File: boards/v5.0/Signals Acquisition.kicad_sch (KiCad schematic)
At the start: 11 parts, among them U3 PC817

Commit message: Update board v5.0 docs
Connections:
- net GND renamed Earth
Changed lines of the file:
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@@
   (junction (at 74.93 92.71) (diameter 0) (color 0 0 0 0)
   )
+  (junction (at 123.19 74.93) (diameter 0) (color 0 0 0 0)
+  )
   (junction (at 113.03 74.93) (diameter 0) (color 0 0 0 0)
   )
@@
     (stroke (width 0) (type default))
   )
+  (wire (pts (xy 123.19 74.93) (xy 123.19 76.2))
+    (stroke (width 0) (type default))
+  )
   (wire (pts (xy 74.93 92.71) (xy 76.2 92.71))
     (stroke (width 0) (type default))
   )
-  (wire (pts (xy 111.76 69.85) (xy 121.92 69.85))
+  (wire (pts (xy 111.76 69.85) (xy 124.46 69.85))
     (stroke (width 0) (type default))
   )
@@
     (stroke (width 0) (type default))
   )
+  (wire (pts (xy 124.46 74.93) (xy 123.19 74.93))
+    (stroke (width 0) (type default))
+  )
   (wire (pts (xy 73.66 130.81) (xy 76.2 130.81))
     (stroke (width 0) (type default))
@@
   )
   (wire (pts (xy 85.09 78.74) (xy 86.36 78.74))
+    (stroke (width 0) (type default))
+  )
+  (wire (pts (xy 123.19 74.93) (xy 121.92 74.93))
     (stroke (width 0) (type default))
   )
@@
     (effects (font (size 1.27 1.27)) (justify left))
   )
-  (hierarchical_label "Vcc" (shape input) (at 121.92 69.85 0) (fields_autoplaced)
+  (hierarchical_label "Vcc" (shape input) (at 124.46 69.85 0) (fields_autoplaced)
     (effects (font (size 1.27 1.27)) (justify left))
   )
@@
     (effects (font (size 1.27 1.27)) (justify left))
   )
-  (hierarchical_label "GND" (shape input) (at 121.92 74.93 0) (fields_autoplaced)
+  (hierarchical_label "GND" (shape input) (at 124.46 74.93 0) (fields_autoplaced)
     (effects (font (size 1.27 1.27)) (justify left))
   )
@@
     )
   )
+  (symbol (lib_id "power:Earth") (at 123.19 76.2 0) (unit 1)
+    (in_bom yes) (on_board yes) (dnp no) (fields_autoplaced)
+    (property "Reference" "#PWR017" (at 123.19 82.55 0)
+      (effects (font (size 1.27 1.27)) hide)
+    )
+    (property "Value" "Earth" (at 123.19 80.01 0)
+      (effects (font (size 1.27 1.27)) hide)
+    )
+    (property "Footprint" "" (at 123.19 76.2 0)
+      (effects (font (size 1.27 1.27)) hide)
+    )
+    (property "Datasheet" "~" (at 123.19 76.2 0)
+      (effects (font (size 1.27 1.27)) hide)
+    )
+    (pin "1")
+    (instances
+      (project "board"
+        (path "/7fdecbff-7204-4ee7-8cff-285fbd7a00a8/99e862ea-0608-4359-a6b2-c0a50691ba5c"
+          (reference "#PWR017") (unit 1)
+        )
+      )
+    )
+  )
   (symbol (lib_id "Diode:1N4007") (at 81.28 78.74 0) (mirror x) (unit 1)
     (in_bom yes) (on_board yes) (dnp no)
@@
   (symbol (lib_id "Isolator:PC817") (at 104.14 72.39 0) (unit 1)
     (in_bom yes) (on_board yes) (dnp no)
-    (property "Reference" "U3" (at 104.14 80.01 0)
-      (effects (font (size 1.27 1.27)))
-    )
-    (property "Value" "PC817" (at 104.14 77.47 0)
-      (effects (font (size 1.27 1.27)))
-    )
+    (property "Reference" "U3" (at 104.14 64.77 0)
+      (effects (font (size 1.27 1.27)))
+    )
+    (property "Value" "PC817" (at 104.14 67.31 0)
+      (effects (font (size 1.27 1.27)))
+    )

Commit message: Update in the V5 board
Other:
- note removed: "-30 to +100"
- note removed: "-40 to +60"
- note removed: "0"
- note removed: "0 to +70"
- note removed: "0 to 1000"
- note removed: "1"
- note removed: "1 to 2"
- note removed: "127Vac"
- note removed: "180kΩ"
- note removed: "2"
- note removed: "220Vac"
- note removed: "3"
- note removed: "300kΩ"
- note removed: "380Vac"
- note removed: "440Vac"
- note removed: "470kΩ"
- note removed: "510kΩ"
- note removed: "After selecting the ideal resistor for your application, according to the table, remember to modify the value of the variable "VOLTAGE_TYPE" in the Microcomputer according to what's in the table"
- note removed: "Input Voltage Range"
- note removed: "Observation"
- note removed: "Operating Temperature Range"
- note removed: "PC817 Operation Temperature"
- note removed: "Rating"
- note removed: "Resistor to Voltage"
- note removed: "Rvolt"
- note removed: "Specifications"
- note removed: "System Voltage (RMS)"
- note removed: "Type"
- note removed: "Unit"
- note removed: "Vac"
- note removed: "Value"
- note removed: "ZMPT101B Nominal Current Range"
- note removed: "ZMPT101B Operation Temperature"
- note removed: "mA"
- note removed: "°C"

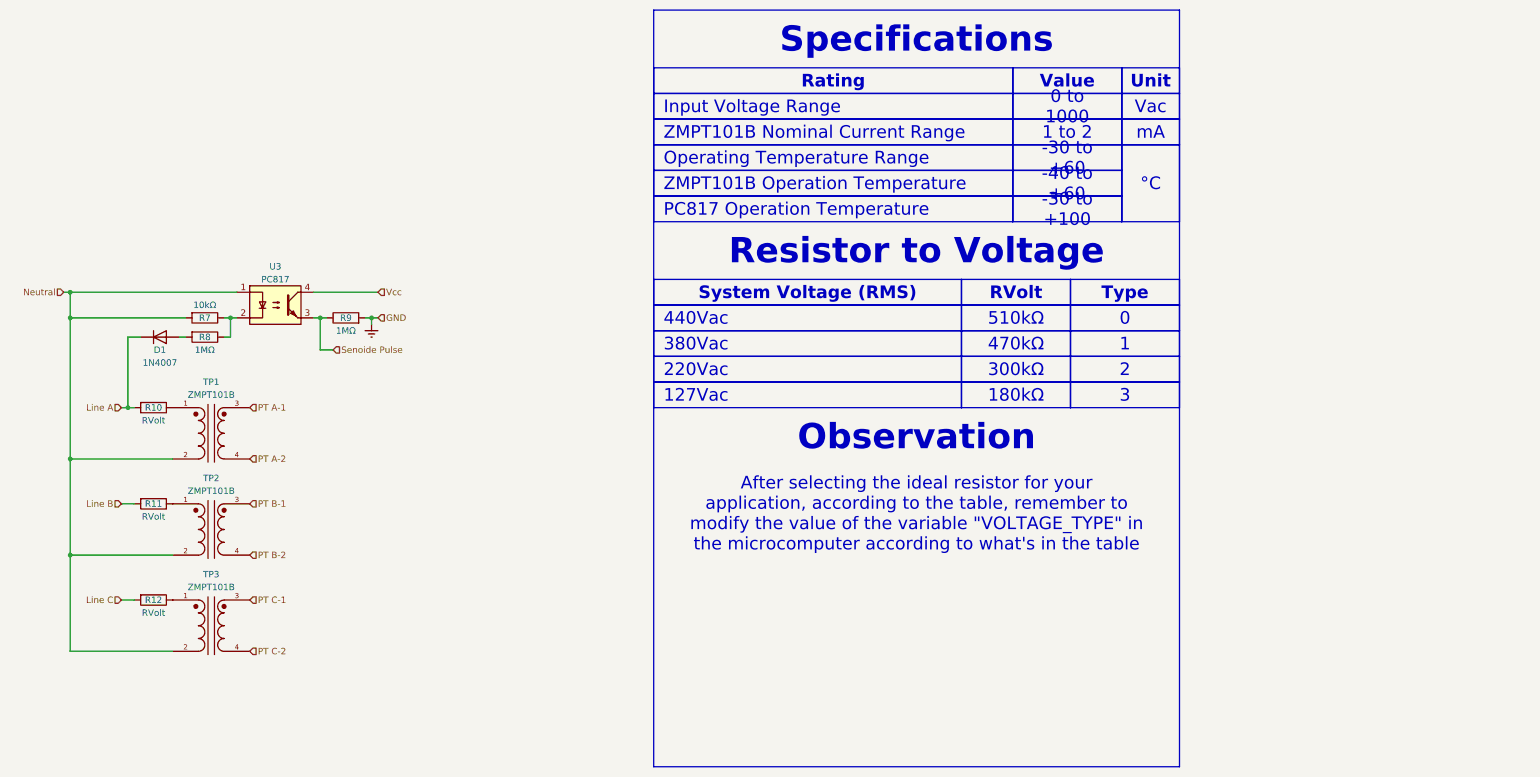
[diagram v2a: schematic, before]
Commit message: Add Jupyter notebook for calculating possible sample rates
- Introduced a new notebook `possible_sample_rates.ipynb` that calculates sample rates based on a base frequency of 60Hz.
- The notebook iterates through a range of values to compute and print sample rates, frequencies, microseconds, and remainders for specific conditions.
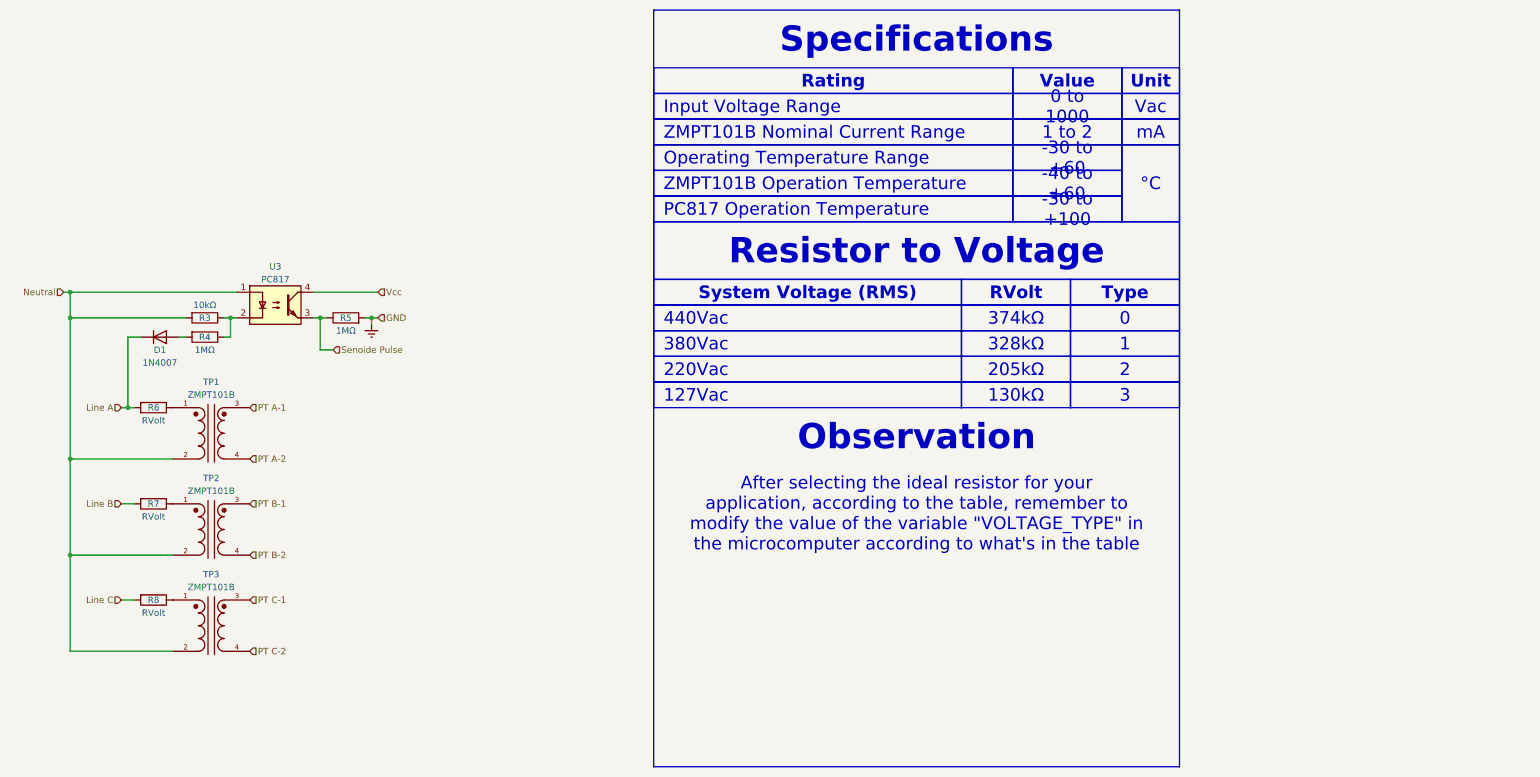
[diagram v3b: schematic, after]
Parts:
- renumbered R7 to R3, R8 to R4, R9 to R5, R10 to R6, R11 to R7, R12 to R8
